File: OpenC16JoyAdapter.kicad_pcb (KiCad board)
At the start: 2 copper layers, 30.5 x 40.6 mm, 9 parts, among them J1 DB9 Male, P1 TO_C16_MINI_DIN_8, P2 PIN5_POWER, P3 OSHW_LOGO_PLACEHOLDER, P4 PULL_UP, U1 74LS244

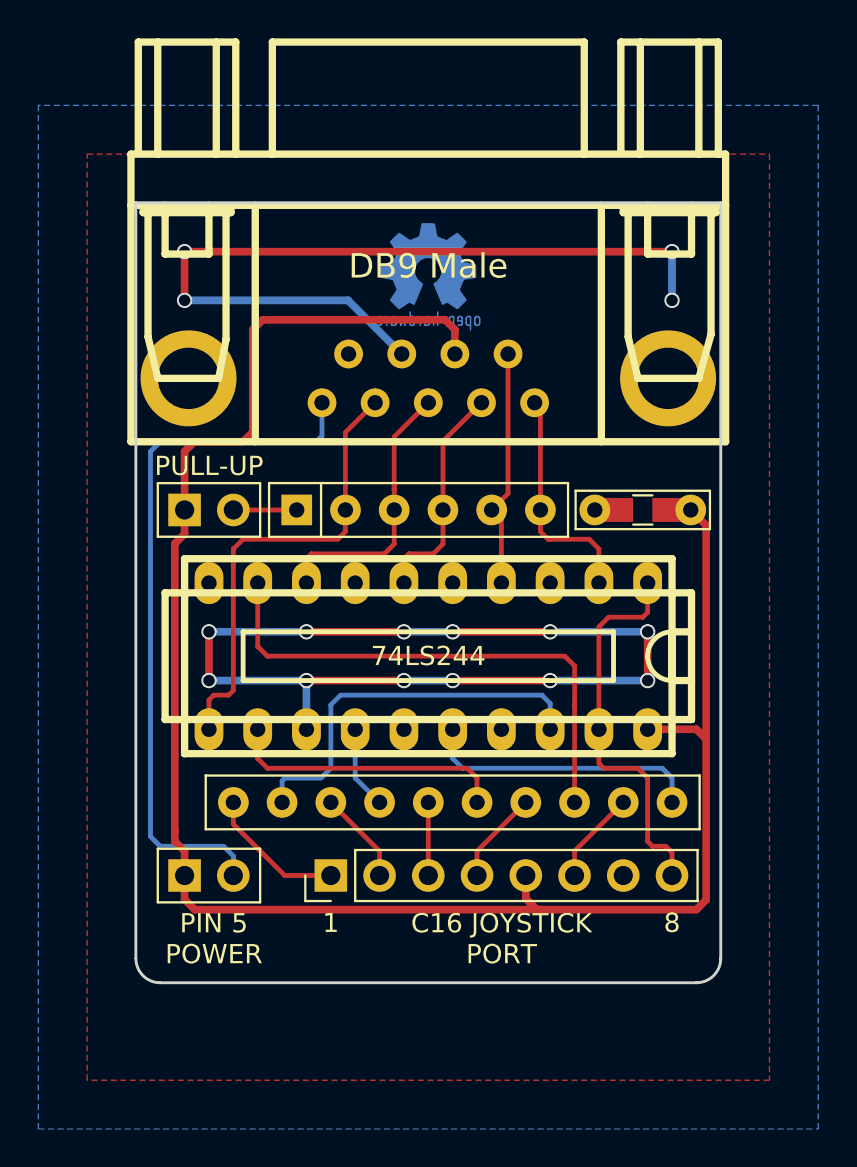
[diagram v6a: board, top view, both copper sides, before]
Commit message: Make power track wider
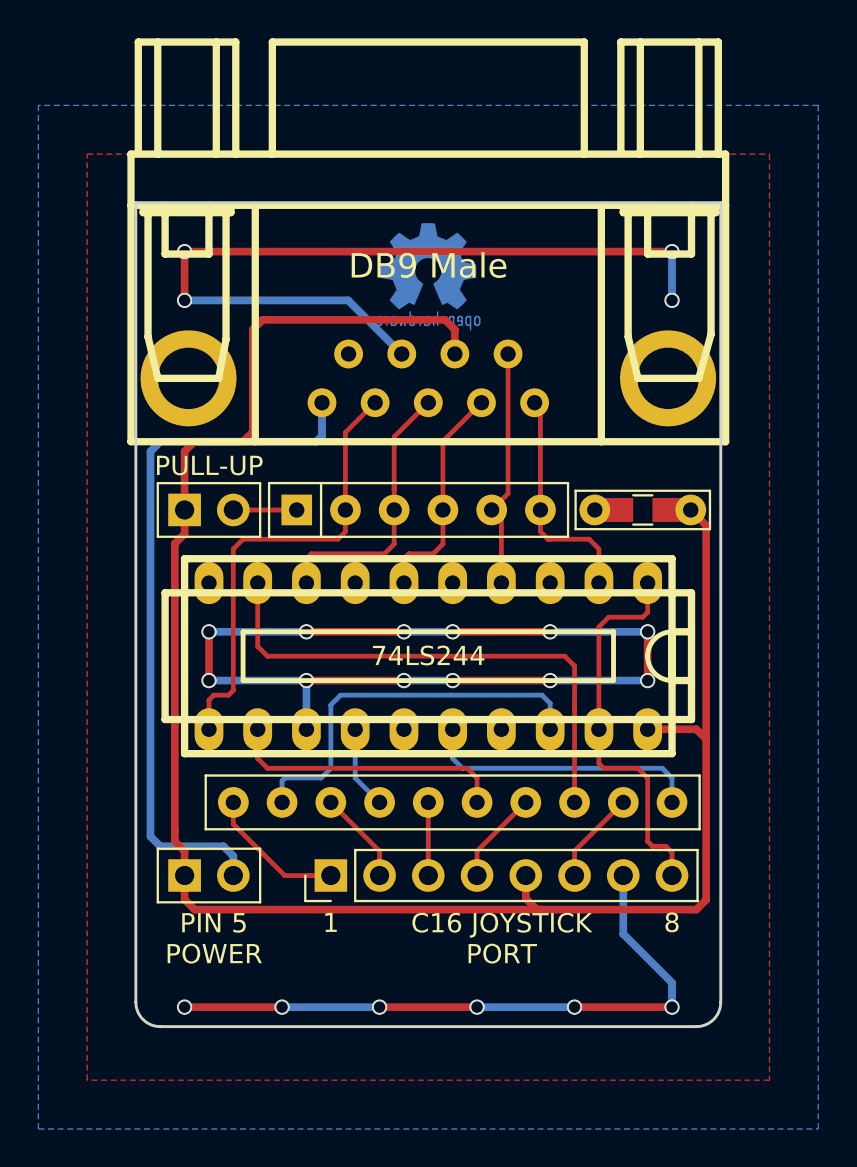
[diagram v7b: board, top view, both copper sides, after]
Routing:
- net GND: track 96.3 -> 129.6 mm, vias 16 -> 22
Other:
- board size 30.5 x 40.6 mm -> 30.5 x 42.9 mm
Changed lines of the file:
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@@
   (general
     (links 37)
-    (no_connects 7)
-    (area 132.004999 91.364999 162.635001 132.155001)
+    (no_connects 0)
+    (area 132.004999 91.364999 162.635001 134.441001)
     (thickness 1.6)
     (drawings 15)
-    (tracks 168)
+    (tracks 182)
     (zones 0)
     (modules 9)
@@
   (title_block
     (title "Open Joystick Adapter for C-16, C-116 and Plus/4")
-    (date 2017-09-27)
-    (rev 1.1)
+    (date 2018-01-01)
+    (rev 2)
     (company SukkoPera)
     (comment 1 http://www.commodore.ca/manuals/funet/cbm/documents/projects/interfaces/plus4joy/plus4joy.html)
@@
     (39 F.Mask user)
     (44 Edge.Cuts user)
-    (49 F.Fab user hide)
+    (49 F.Fab user)
   )
   (setup
@@
     (add_net /md_right)
     (add_net /md_up)
-    (add_net "Net-(J1-Pad5)")
     (add_net "Net-(P4-Pad2)")
     (add_net "Net-(RN2-Pad1)")
@@
     (add_net +5V)
     (add_net GND)
+    (add_net "Net-(J1-Pad5)")
   )
   (module conn_d-sub:DB_9M (layer F.Cu)
@@
     (effects (font (size 1.5 1.5) (thickness 0.3)) (justify mirror))
   )
-  (gr_arc (start 161.29 130.81) (end 162.56 130.81) (angle 90) (layer Edge.Cuts) (width 0.15))
-  (gr_arc (start 133.35 130.81) (end 133.35 132.08) (angle 90) (layer Edge.Cuts) (width 0.15))
-  (gr_text github.com/SukkoPera/OpenC16JoyAdapter (at 147.32 129.286) (layer B.SilkS)
+  (gr_arc (start 161.29 133.096) (end 162.56 133.096) (angle 90) (layer Edge.Cuts) (width 0.15))
+  (gr_arc (start 133.35 133.096) (end 133.35 134.366) (angle 90) (layer Edge.Cuts) (width 0.15))
+  (gr_text github.com/SukkoPera/OpenC16JoyAdapter (at 147.32 130.048) (layer B.SilkS)
     (effects (font (size 1 0.85) (thickness 0.15)) (justify mirror))
   )
   (dimension 30.48 (width 0.3) (layer F.Fab)
-    (gr_text "30,480 mm" (at 147.342447 137.477688) (layer F.Fab)
+    (gr_text "30,480 mm" (at 147.32 140.796) (layer F.Fab)
       (effects (font (size 1.5 1.5) (thickness 0.3)))
     )
-    (feature1 (pts (xy 132.102447 131.047688) (xy 132.102447 138.827688)))
-    (feature2 (pts (xy 162.582447 131.047688) (xy 162.582447 138.827688)))
-    (crossbar (pts (xy 162.582447 136.127688) (xy 132.102447 136.127688)))
-    (arrow1a (pts (xy 132.102447 136.127688) (xy 133.228951 135.541267)))
-    (arrow1b (pts (xy 132.102447 136.127688) (xy 133.228951 136.714109)))
-    (arrow2a (pts (xy 162.582447 136.127688) (xy 161.455943 135.541267)))
-    (arrow2b (pts (xy 162.582447 136.127688) (xy 161.455943 136.714109)))
+    (feature1 (pts (xy 132.08 134.366) (xy 132.08 142.146)))
+    (feature2 (pts (xy 162.56 134.366) (xy 162.56 142.146)))
+    (crossbar (pts (xy 162.56 139.446) (xy 132.08 139.446)))
+    (arrow1a (pts (xy 132.08 139.446) (xy 133.206504 138.859579)))
+    (arrow1b (pts (xy 132.08 139.446) (xy 133.206504 140.032421)))
+    (arrow2a (pts (xy 162.56 139.446) (xy 161.433496 138.859579)))
+    (arrow2b (pts (xy 162.56 139.446) (xy 161.433496 140.032421)))
   )
   (gr_text 8 (at 160.02 128.969) (layer F.SilkS)
@@
     (effects (font (size 1 1) (thickness 0.15)))
   )
-  (dimension 39.624 (width 0.3) (layer F.Fab)
-    (gr_text "39,624 mm" (at 176.61 111.252 270) (layer F.Fab)
+  (dimension 42.926 (width 0.3) (layer F.Fab)
+    (gr_text "42,926 mm" (at 176.61 112.903 270) (layer F.Fab)
       (effects (font (size 1.5 1.5) (thickness 0.3)))
     )
-    (feature1 (pts (xy 162.56 131.064) (xy 177.96 131.064)))
+    (feature1 (pts (xy 162.56 134.366) (xy 177.96 134.366)))
     (feature2 (pts (xy 162.56 91.44) (xy 177.96 91.44)))
-    (crossbar (pts (xy 175.26 91.44) (xy 175.26 131.064)))
-    (arrow1a (pts (xy 175.26 131.064) (xy 174.673579 129.937496)))
-    (arrow1b (pts (xy 175.26 131.064) (xy 175.846421 129.937496)))
+    (crossbar (pts (xy 175.26 91.44) (xy 175.26 134.366)))
+    (arrow1a (pts (xy 175.26 134.366) (xy 174.673579 133.239496)))
+    (arrow1b (pts (xy 175.26 134.366) (xy 175.846421 133.239496)))
     (arrow2a (pts (xy 175.26 91.44) (xy 174.673579 92.566504)))
     (arrow2b (pts (xy 175.26 91.44) (xy 175.846421 92.566504)))
   )
-  (gr_line (start 132.08 130.81) (end 132.08 91.44) (layer Edge.Cuts) (width 0.15))
-  (gr_line (start 161.29 132.08) (end 133.35 132.08) (layer Edge.Cuts) (width 0.15))
-  (gr_line (start 162.56 91.44) (end 162.56 130.81) (layer Edge.Cuts) (width 0.15))
+  (gr_line (start 132.08 133.096) (end 132.08 91.44) (layer Edge.Cuts) (width 0.15))
+  (gr_line (start 161.29 134.366) (end 133.35 134.366) (layer Edge.Cuts) (width 0.15))
+  (gr_line (start 162.56 91.44) (end 162.56 133.096) (layer Edge.Cuts) (width 0.15))
   (gr_line (start 132.08 91.44) (end 162.56 91.44) (layer Edge.Cuts) (width 0.15))
   (segment (start 134.62 107.442) (end 134.62 104.394) (width 0.4) (layer F.Cu) (net 1))
@@
   (segment (start 152.4 127.694081) (end 152.975919 128.27) (width 0.4) (layer F.Cu) (net 1))
   (segment (start 152.975919 128.27) (end 153.162 128.27) (width 0.4) (layer F.Cu) (net 1))
+  (segment (start 160.02 133.35) (end 160.02 132.08) (width 0.4) (layer B.Cu) (net 2))
+  (segment (start 160.02 132.08) (end 157.48 129.54) (width 0.4) (layer B.Cu) (net 2))
+  (segment (start 157.48 129.54) (end 157.48 126.492) (width 0.4) (layer B.Cu) (net 2))
+  (segment (start 139.7 133.35) (end 134.62 133.35) (width 0.4) (layer F.Cu) (net 2))
+  (via (at 134.62 133.35) (size 0.8) (drill 0.6) (layers F.Cu B.Cu) (net 2))
+  (segment (start 144.78 133.35) (end 139.7 133.35) (width 0.4) (layer B.Cu) (net 2))
+  (via (at 139.7 133.35) (size 0.8) (drill 0.6) (layers F.Cu B.Cu) (net 2))
+  (segment (start 149.86 133.35) (end 144.78 133.35) (width 0.4) (layer F.Cu) (net 2))
+  (via (at 144.78 133.35) (size 0.8) (drill 0.6) (layers F.Cu B.Cu) (net 2))
+  (segment (start 154.94 133.35) (end 149.86 133.35) (width 0.4) (layer B.Cu) (net 2))
+  (via (at 149.86 133.35) (size 0.8) (drill 0.6) (layers F.Cu B.Cu) (net 2))
+  (segment (start 160.02 133.35) (end 154.94 133.35) (width 0.4) (layer F.Cu) (net 2))
+  (via (at 154.94 133.35) (size 0.8) (drill 0.6) (layers F.Cu B.Cu) (net 2))
+  (via (at 160.02 133.35) (size 0.8) (drill 0.6) (layers F.Cu B.Cu) (net 2))
   (segment (start 160.02 93.98) (end 160.02 96.52) (width 0.4) (layer B.Cu) (net 2))
   (via (at 160.02 96.52) (size 0.8) (drill 0.6) (layers F.Cu B.Cu) (net 2))
@@
   (via (at 140.97 116.332) (size 0.8) (drill 0.6) (layers F.Cu B.Cu) (net 2))
   (via (at 140.97 113.792) (size 0.8) (drill 0.6) (layers F.Cu B.Cu) (net 2))
-  (segment (start 137.16 126.492) (end 137.16 125.476) (width 0.25) (layer B.Cu) (net 3))
-  (segment (start 137.16 125.476) (end 136.652 124.968) (width 0.25) (layer B.Cu) (net 3))
-  (segment (start 133.35 124.968) (end 132.842 124.46) (width 0.25) (layer B.Cu) (net 3))
-  (segment (start 133.35 103.886) (end 141.478 103.886) (width 0.25) (layer B.Cu) (net 3))
-  (segment (start 141.478 103.886) (end 141.78026 103.58374) (width 0.25) (layer B.Cu) (net 3))
-  (segment (start 141.78026 103.58374) (end 141.78026 101.854) (width 0.25) (layer B.Cu) (net 3))
-  (segment (start 136.652 124.968) (end 133.35 124.968) (width 0.25) (layer B.Cu) (net 3))
-  (segment (start 132.842 124.46) (end 132.842 104.394) (width 0.25) (layer B.Cu) (net 3))
-  (segment (start 132.842 104.394) (end 133.35 103.886) (width 0.25) (layer B.Cu) (net 3))
+  (segment (start 137.16 126.492) (end 137.16 125.476) (width 0.4) (layer B.Cu) (net 3))
+  (segment (start 137.16 125.476) (end 136.652 124.968) (width 0.4) (layer B.Cu) (net 3))
+  (segment (start 133.35 124.968) (end 132.842 124.46) (width 0.4) (layer B.Cu) (net 3))
+  (segment (start 133.35 103.886) (end 141.478 103.886) (width 0.4) (layer B.Cu) (net 3))
+  (segment (start 141.478 103.886) (end 141.78026 103.58374) (width 0.4) (layer B.Cu) (net 3))
+  (segment (start 141.78026 103.58374) (end 141.78026 101.854) (width 0.4) (layer B.Cu) (net 3))
+  (segment (start 136.652 124.968) (end 133.35 124.968) (width 0.4) (layer B.Cu) (net 3))
+  (segment (start 132.842 124.46) (end 132.842 104.394) (width 0.4) (layer B.Cu) (net 3))
+  (segment (start 132.842 104.394) (end 133.35 103.886) (width 0.4) (layer B.Cu) (net 3))
   (segment (start 145.542 103.632) (end 145.542 106.172) (width 0.25) (layer F.Cu) (net 4))
   (segment (start 145.542 106.172) (end 145.542 106.426) (width 0.25) (layer F.Cu) (net 4))
